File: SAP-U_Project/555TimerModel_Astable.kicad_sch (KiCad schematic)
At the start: 11 parts, among them Q1 BC107, U1 Comparator 2, U2 SR LATCH

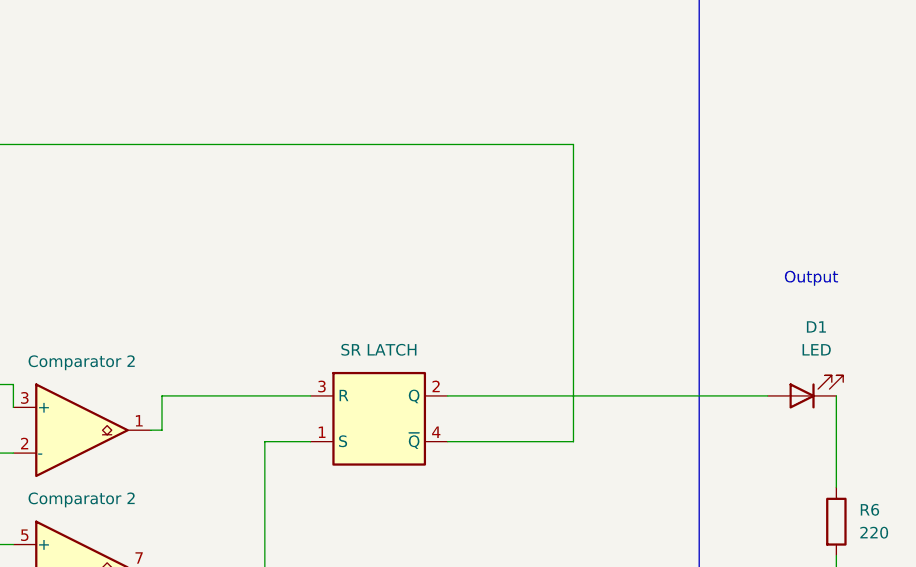
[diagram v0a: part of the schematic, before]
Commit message: Checkpoint: added circuit for Bistable
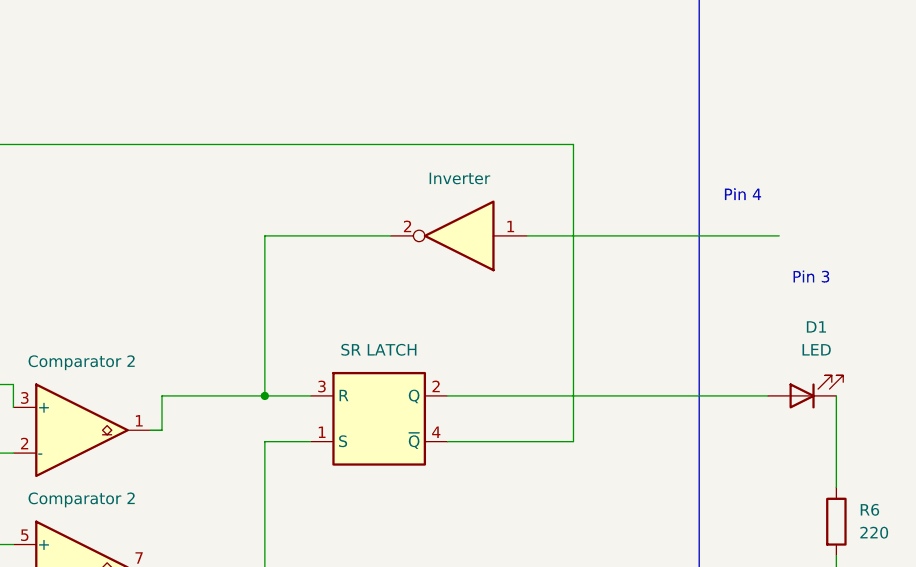
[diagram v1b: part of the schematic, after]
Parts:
- added U11: Inverter, symbol 74xx:74LS04
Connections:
- net at U1.1, U2.3 (R): now also U11.2
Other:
- note added: "Pin 3"
- note added: "Pin 4"
- note removed: "Output"
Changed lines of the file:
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@@
+	)
+	(junction
+		(at 132.08 96.52)
+		(diameter 0)
+		(color 0 0 0 0)
 	)
 	(junction
@@
 	(wire
 		(pts
+			(xy 146.05 78.74) (xy 132.08 78.74)
+		)
+		(stroke
+			(width 0)
+			(type default)
+		)
+	)
+	(wire
+		(pts
 			(xy 104.14 118.11) (xy 53.34 118.11)
 		)
@@
 	(wire
 		(pts
+			(xy 132.08 78.74) (xy 132.08 96.52)
+		)
+		(stroke
+			(width 0)
+			(type default)
+		)
+	)
+	(wire
+		(pts
+			(xy 132.08 96.52) (xy 137.16 96.52)
+		)
+		(stroke
+			(width 0)
+			(type default)
+		)
+	)
+	(wire
+		(pts
 			(xy 74.93 73.66) (xy 74.93 77.47)
 		)
@@
 	(wire
 		(pts
+			(xy 161.29 78.74) (xy 189.23 78.74)
+		)
+		(stroke
+			(width 0)
+			(type default)
+		)
+	)
+	(wire
+		(pts
 			(xy 87.63 113.03) (xy 104.14 113.03)
 		)
@@
 	(wire
 		(pts
-			(xy 120.65 96.52) (xy 137.16 96.52)
+			(xy 120.65 96.52) (xy 132.08 96.52)
 		)
 		(stroke
@@
 		)
 	)
-	(text "Output\n"
+	(text "Pin 3"
 		(exclude_from_sim no)
 		(at 192.786 83.566 0)
@@
 		)
 	)
+	(text "Pin 4\n"
+		(exclude_from_sim no)
+		(at 185.166 74.422 0)
+		(effects
+			(font
+				(size 1.27 1.27)
+				(color 72 0 0 1)
+			)
+		)
+	)
 	(symbol
 		(lib_id "power:GND")
@@
 					(unit 1)
 				)
+			)
+		)
+	)
+	(symbol
+		(lib_id "74xx:74LS04")
+		(at 153.67 78.74 180)
+		(unit 1)
+		(exclude_from_sim no)
+		(in_bom yes)
+		(on_board yes)
+		(dnp no)
+		(fields_autoplaced yes)
+		(property "Reference" "U11"
+			(at 153.67 69.85 0)
+			(effects
+				(font
+					(size 1.27 1.27)
+				)
+				(hide yes)
+			)
+		)
+		(property "Value" "Inverter"
+			(at 153.67 72.39 0)
+			(effects
+				(font
+					(size 1.27 1.27)
+				)
+			)
+		)
+		(property "Footprint" ""
+			(at 153.67 78.74 0)
+			(effects
+				(font
+					(size 1.27 1.27)
+				)
+				(hide yes)
+			)
+		)
+		(property "Datasheet" "http://www.ti.com/lit/gpn/sn74LS04"
+			(at 153.67 78.74 0)
+			(effects
+				(font
+					(size 1.27 1.27)
+				)
+				(hide yes)
+			)
+		)
+		(property "Description" "Hex Inverter"
+			(at 153.67 78.74 0)
+			(effects
+				(font
+					(size 1.27 1.27)
+				)
+				(hide yes)
+			)
+		)
+		(pin "14"
+		)
+		(pin "5"
+		)
+		(pin "13"
+		)
+		(pin "6"
+		)
+		(pin "7"
+		)
+		(pin "12"
+		)
+		(pin "3"
+		)
+		(pin "11"
+		)
+		(pin "8"
+		)
+		(pin "4"
+		)
+		(pin "10"
+		)
+		(pin "9"
+		)
+		(pin "1"
+		)
+		(pin "2"
+		)
+		(instances
+			(project "SAP-U_Project"
+				(path "/e63e39d7-6ac0-4ffd-8aa3-1841a4541b55/7f1b9d87-3d1d-4a5d-8055-cfab36c6883b/de256fc7-e535-482a-9ac7-7c096b97e8b9"
+					(reference "U11")
+					(unit 1)
+				)

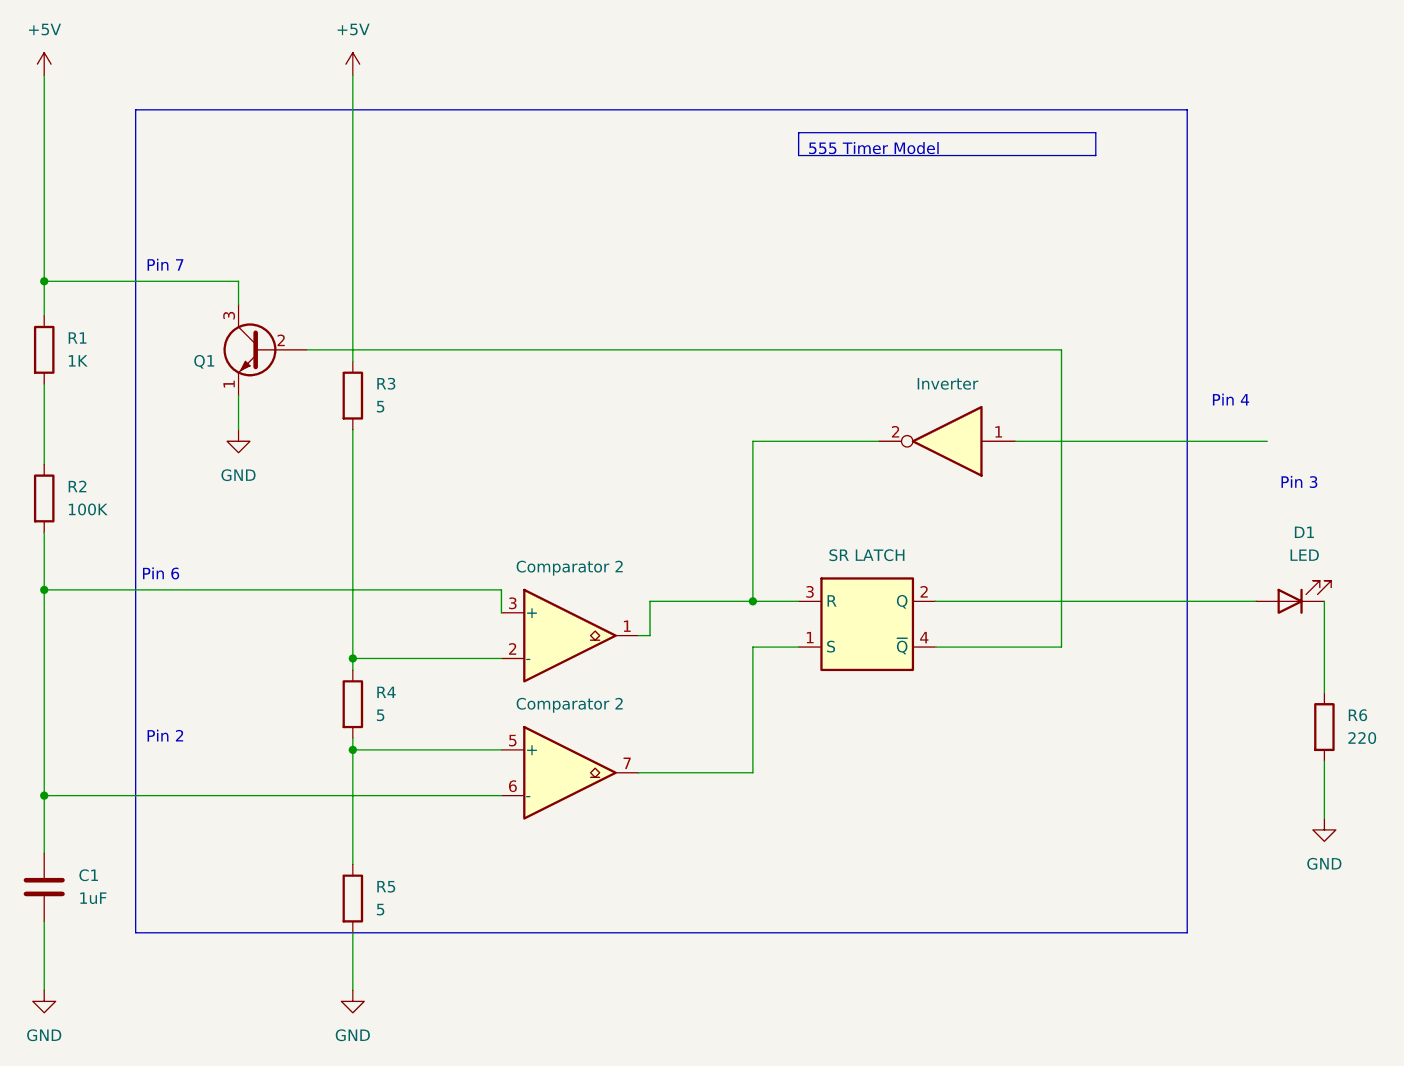
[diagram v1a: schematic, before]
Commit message: Checkpoint: added switching logic
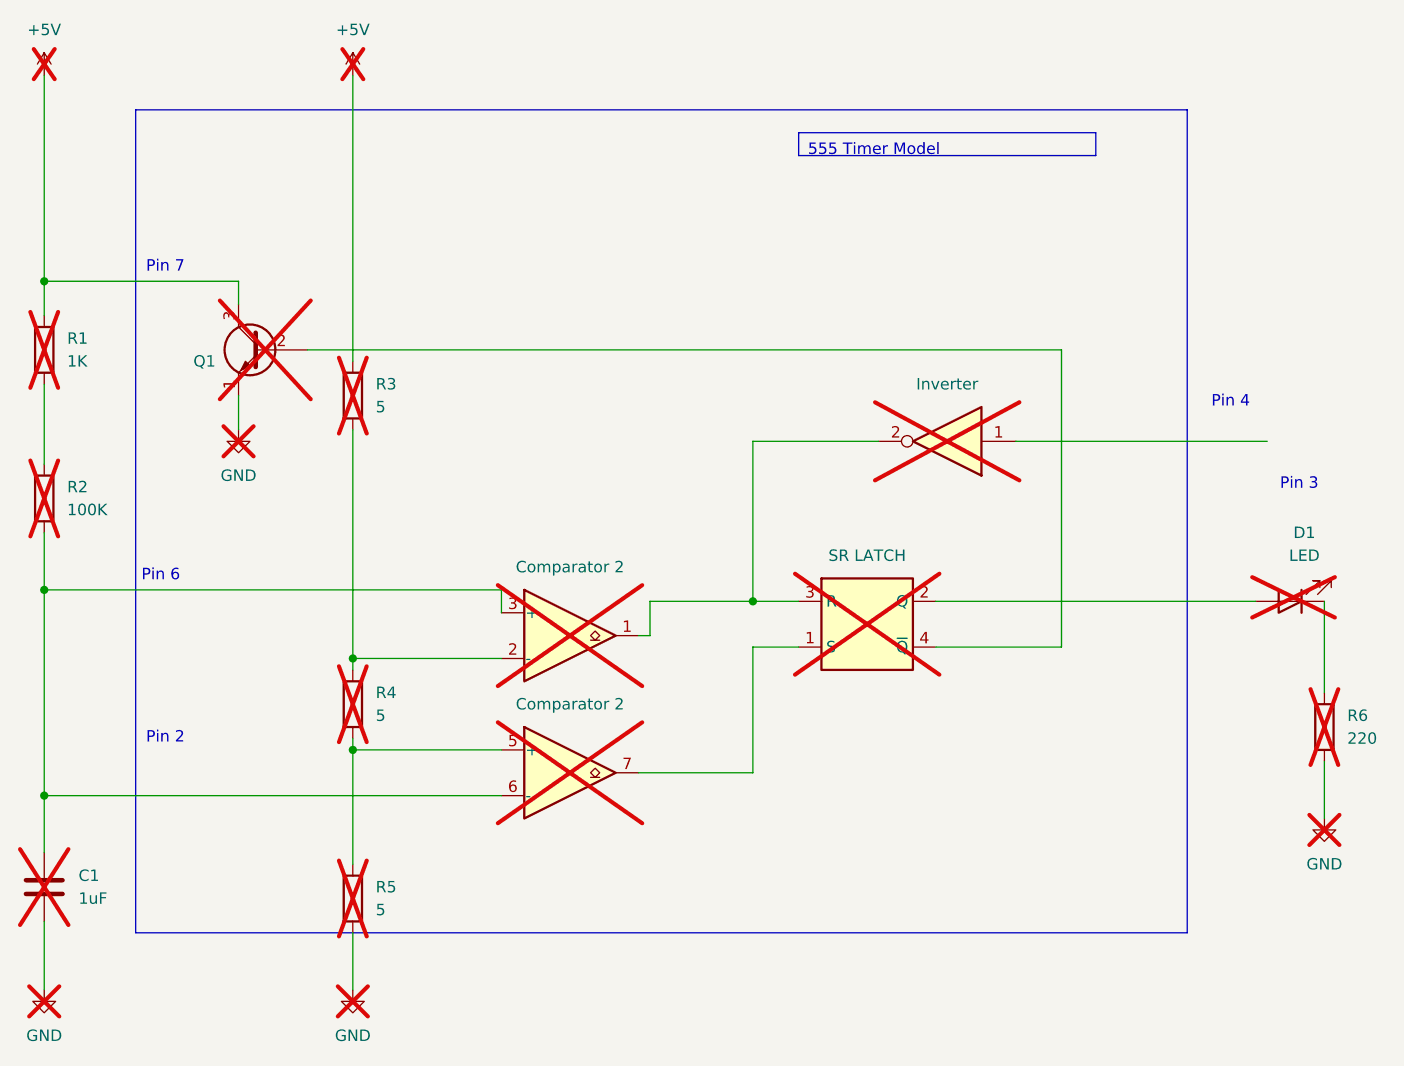
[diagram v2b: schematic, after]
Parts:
- C1, D1, Q1, R1, R2, R3, R4, R5, R6, U1, U2: now not fitted
- U11: now not fitted; now left out of the parts list
